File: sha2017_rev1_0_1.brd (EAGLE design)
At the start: 95 x 86 mm, 201 parts, among them IC1 CP210X_USB_UART, IC2 LD117AS33TR, IC3 ESP32WROOM32, IC4 TP4056, M1 MOTOR10MM, Q1 MMBT2222A, Q2 MMBT2222A, Q3 MMBT2222A, Q4 MMBT2222A, Q5 SI1304 BDL, Q6 MMBT2222A, U1 MPR121QR2, X2 2908-05WB-MG, X4 JST-PH3

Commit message: Add option for GD/DKE displays - TODO: ROUTE
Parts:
- added C42: 1u, sha2017_rev0_1_0_dev:C0603-DASHES
- added R26: 0R, sha2017_rev0_1_0_dev:R0603-DASHES
- L1: value 22µ -> 47µ
- R19: value 5R -> 2R7
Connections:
- new net LCD_VDD: C42.1, R26.2, X1.7
- net +3V3: now also R26.1; no longer X1.7
- net GND: now also C42.2
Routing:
- net +3V3: track 232.9 -> 227.1 mm

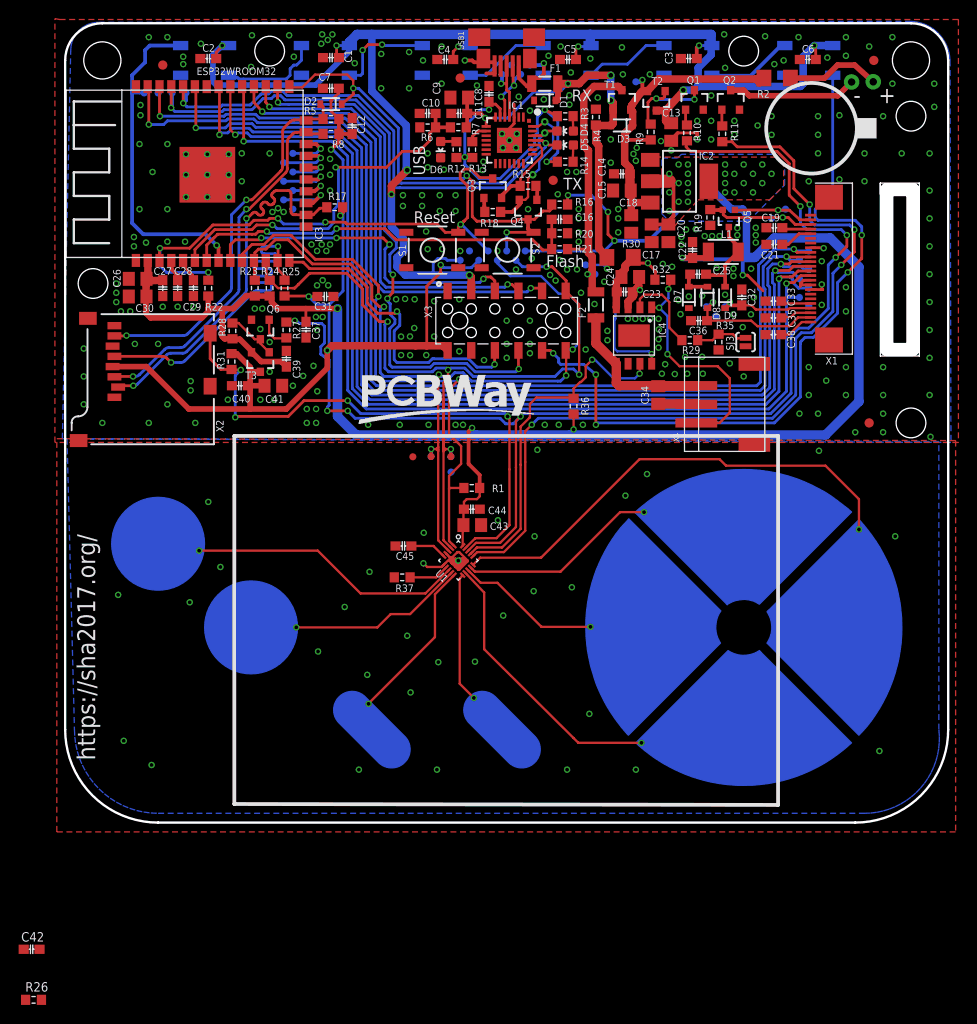
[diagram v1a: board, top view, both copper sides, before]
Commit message: routing of display option
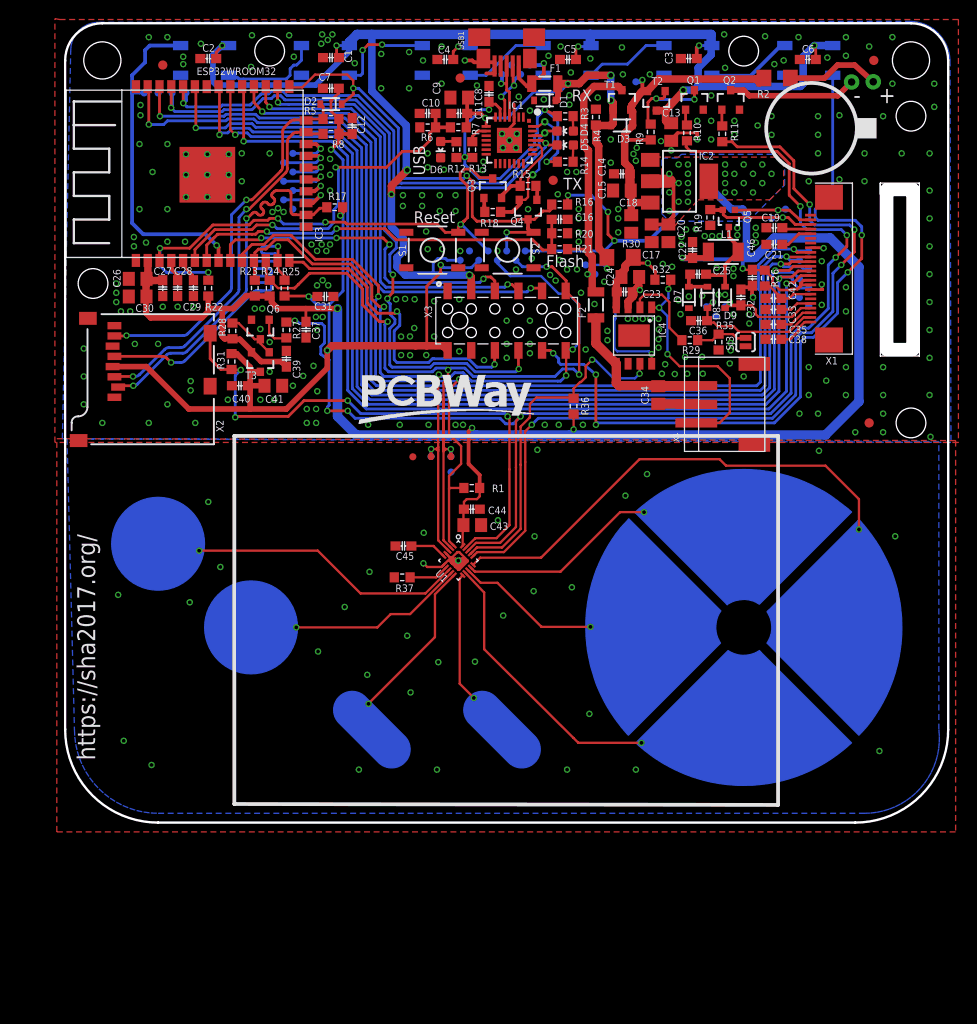
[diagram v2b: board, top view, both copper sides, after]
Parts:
- added C46: 1u, sha2017_rev0_1_0_dev:C0603-DASHES
- moved R26 110.5 mm to (75.3, 57.6), turned to 270 degrees
- moved C42 106.2 mm to (76.2, 55.4), turned to 180 degrees
- moved C33 0.90 mm to (76.2, 54.2)
- moved C35 0.70 mm to (76.2, 52.6)
- moved C38 0.50 mm to (76.2, 51.0)
- moved C32 0.10 mm to (72.7, 55.5)
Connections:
- net +3V3: now also C46.1
- net GND: now also C46.2
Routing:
- net LCD_VDD: track 0.00 -> 5.71 mm
- net +3V3: track 227.1 -> 231.4 mm
- net GND: track 42.1 -> 44.6 mm, vias 306 -> 308
- net PREVGH: track 11.1 -> 12.1 mm
- net VCOM: track 3.71 -> 4.54 mm
- net VSL: track 3.37 -> 4.12 mm
- net PREVGL: track 14.9 -> 15.4 mm

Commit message: FINAL gerbers, design freeze
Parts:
- F1, F2: value 900mA -> 1A
- IC2: value LD117AS33TR -> AP2114H
- R30: value 0R27 -> 0R27 1/4W
- moved $$U$2 1.32 mm to (90.6, 30.0)
- moved U$17 1.17 mm to (88.6, 6.10)
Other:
- board text added: "Brought to you by: Anne Jan Brouwer Bas van Sisseren Gavan Fantom Jeroen Domburg Markus Bechtold Niek Blankers Sebastian Oort Thomas Roos"
- board text added: "CAUTION: DO NOT LOOK INTO LEDS WITH REMAINING EYE"
- board text added: "Do not touch"
- board text added: "SHA2017"
- board text added: "Still Hacking Anyway"
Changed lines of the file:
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@@
 <setting verticaltext="up"/>
 </settings>
-<grid distance="0.1" unitdist="mm" unit="mm" style="lines" multiple="1" display="yes" altdistance="0.025" altunitdist="inch" altunit="inch"/>
+<grid distance="0.25" unitdist="mm" unit="mm" style="lines" multiple="1" display="yes" altdistance="0.025" altunitdist="inch" altunit="inch"/>
 <layers>
 <layer number="1" name="Top" color="4" fill="1" visible="yes" active="yes"/>
@@
 <layer number="21" name="tPlace" color="7" fill="1" visible="yes" active="yes"/>
 <layer number="22" name="bPlace" color="7" fill="1" visible="yes" active="yes"/>
-<layer number="23" name="tOrigins" color="15" fill="1" visible="yes" active="yes"/>
-<layer number="24" name="bOrigins" color="15" fill="1" visible="yes" active="yes"/>
+<layer number="23" name="tOrigins" color="15" fill="1" visible="no" active="yes"/>
+<layer number="24" name="bOrigins" color="15" fill="1" visible="no" active="yes"/>
 <layer number="25" name="tNames" color="7" fill="1" visible="yes" active="yes"/>
-<layer number="26" name="bNames" color="7" fill="1" visible="no" active="yes"/>
+<layer number="26" name="bNames" color="7" fill="1" visible="yes" active="yes"/>
 <layer number="27" name="tValues" color="7" fill="1" visible="no" active="yes"/>
 <layer number="28" name="bValues" color="7" fill="1" visible="no" active="yes"/>
-<layer number="29" name="tStop" color="7" fill="3" visible="yes" active="yes"/>
-<layer number="30" name="bStop" color="7" fill="6" visible="yes" active="yes"/>
+<layer number="29" name="tStop" color="7" fill="3" visible="no" active="yes"/>
+<layer number="30" name="bStop" color="7" fill="6" visible="no" active="yes"/>
 <layer number="31" name="tCream" color="7" fill="4" visible="no" active="yes"/>
 <layer number="32" name="bCream" color="7" fill="5" visible="no" active="yes"/>
@@
 <text x="87.5" y="76.4" size="1.778" layer="21" font="vector" ratio="16">+</text>
 <text x="84.8" y="76.4" size="1.778" layer="21" font="vector" ratio="16">-</text>
-<text x="1.3" y="5.7" size="1.9304" layer="25" font="vector" ratio="15" rot="R90" align="top-left">https://sha2017.org/</text>
+<text x="11.7" y="4.2" size="1.9304" layer="25" font="vector" ratio="15" rot="R90" align="top-left">https://sha2017.org/</text>
 <rectangle x1="29.7558" y1="26.0714" x2="29.7802" y2="26.0958" layer="26" rot="R180"/>
 <rectangle x1="29.585" y1="26.0714" x2="29.7314" y2="26.0958" layer="26" rot="R180"/>
@@
 <hole x="42.42" y="53" drill="1.8"/>
 <hole x="52.58" y="53" drill="1.8"/>
+<text x="35.3" y="40.4" size="1.778" layer="26" font="vector" ratio="15" rot="MR0">Brought to you by:
+Anne Jan Brouwer
+Bas van Sisseren
+Gavan Fantom
+Jeroen Domburg
+Markus Bechtold
+Niek Blankers
+Sebastian Oort
+Thomas Roos</text>
+<text x="85.1" y="40.9" size="1.6764" layer="26" font="vector" ratio="15" rot="MR0">Still Hacking Anyway</text>
+<text x="7.7" y="12.7" size="2.54" layer="25" font="vector" ratio="15" rot="R90" align="top-left">SHA2017</text>
+<text x="45.2" y="26.6" size="1.4224" layer="25" font="vector" ratio="15">Do not touch</text>
+<text x="75.1" y="2.5" size="1.4224" layer="25" font="vector" ratio="15" rot="R90">CAUTION:
+DO NOT LOOK INTO LEDS
+WITH REMAINING EYE</text>
+<polygon width="0.3048" layer="21">
+<vertex x="78" y="0.75"/>
+<vertex x="85.5" y="0.75" curve="90"/>
+<vertex x="93" y="8.25"/>
+<vertex x="93" y="40.75"/>
+<vertex x="78" y="40.75"/>
+</polygon>
 </plain>
 <attributes>
@@
 <attribute name="PARTNO" value="GRM21BR61C475KA88K" x="42.4" y="77" size="1.778" layer="27" rot="R180" display="off"/>
 </element>
-<element name="F1" library="SparkFun-PowerIC" package="PTC-1206" value="900mA" x="51.6" y="78.5" smashed="yes">
+<element name="F1" library="SparkFun-PowerIC" package="PTC-1206" value="1A" x="51.6" y="78.5" smashed="yes">
 <attribute name="PROD_ID" value="RES-11150" x="127.8" y="-1.51" size="1.778" layer="27" display="off"/>
 <attribute name="NAME" x="52.126" y="79.77" size="0.8128" layer="25" font="vector" ratio="16"/>
@@
 <attribute name="PARTNO" value="GRM21BR61C475KA88K" x="64.9" y="62.4" size="1.778" layer="27" rot="R270" display="off"/>
 </element>
-<element name="IC2" library="v-reg" package="SOT223" value="LD117AS33TR" x="66.1" y="68" smashed="yes" rot="R270">
+<element name="IC2" library="v-reg" package="SOT223" value="AP2114H" x="66.1" y="68" smashed="yes" rot="R270">
 <attribute name="NAME" x="68.18" y="70.333" size="0.8128" layer="25" font="vector" ratio="16"/>
 <attribute name="VALUE" x="61.7551" y="70.4051" size="1.27" layer="27" rot="R270"/>
@@
 <attribute name="PARTNO" value="ERJ-3GEYJ103V" x="70.7" y="73.1" size="1.778" layer="27" rot="R270" display="off"/>
 </element>
-<element name="F2" library="SparkFun-PowerIC" package="PTC-1206" value="900mA" x="57.1" y="54.7" smashed="yes" rot="R90">
+<element name="F2" library="SparkFun-PowerIC" package="PTC-1206" value="1A" x="57.1" y="54.7" smashed="yes" rot="R90">
 <attribute name="PROD_ID" value="RES-11150" x="34.8" y="36.5" size="1.778" layer="27" rot="R90" display="off"/>
 <attribute name="NAME" x="56.03" y="53.276" size="0.8128" layer="25" font="vector" ratio="16" rot="R90"/>
@@
 <attribute name="PARTNO" value="NAP" x="50.5" y="29.8" size="1.778" layer="27" display="off"/>
 </element>
-<element name="U$17" library="badge" package="VIA" value="VIA" x="87.6" y="6.7" smashed="yes">
-<attribute name="PARTNO" value="NAP" x="87.6" y="6.7" size="1.778" layer="27" display="off"/>
+<element name="U$17" library="badge" package="VIA" value="VIA" x="88.6" y="6.1" smashed="yes">
+<attribute name="PARTNO" value="NAP" x="88.6" y="6.1" size="1.778" layer="27" display="off"/>
 </element>
 <element name="$$U$5" library="badge" package="VIA" value="VIA" x="5.7" y="23.5" smashed="yes">
@@
 <attribute name="PARTNO" value="NAP" x="37.1603" y="13.00475" size="1.778" layer="27" display="off"/>
 </element>
-<element name="$$U$2" library="badge" package="VIA" value="VIA" x="89.3" y="29.8" smashed="yes">
-<attribute name="PARTNO" value="NAP" x="89.3" y="29.8" size="1.778" layer="27" display="off"/>
+<element name="$$U$2" library="badge" package="VIA" value="VIA" x="90.6" y="30" smashed="yes">
+<attribute name="PARTNO" value="NAP" x="90.6" y="30" size="1.778" layer="27" display="off"/>
 </element>
 <element name="TP100" library="SparkFun-Passives" package="PAD.03X.03" value="TEST-POINT3" x="41.5" y="38.38225" smashed="yes" rot="MR0">
@@
 <attribute name="VALUE" x="41.208409375" y="30.98866875" size="2.0828" layer="27" ratio="10" rot="SR315"/>
 </element>
-<element name="R30" library="rcl" package="R1206" value="0R27" x="59.7" y="59.8" smashed="yes">
+<element name="R30" library="rcl" package="R1206" value="0R27 1/4W" x="59.7" y="59.8" smashed="yes">
 <attribute name="PARTNO" value="ERJ-3GEYJ154V" x="59.7" y="59.8" size="1.778" layer="27" display="off"/>
 <attribute name="NAME" x="59.911" y="60.889" size="0.8128" layer="25" font="vector" ratio="15"/>
@@
 </board>
 </drawing>
+<compatibility>
+<note version="6.3" minversion="6.2.2" severity="warning">
+Since Version 6.2.2 text objects can contain more than one line,
+which will not be processed correctly with this version.
+</note>
+</compatibility>
 </eagle>
